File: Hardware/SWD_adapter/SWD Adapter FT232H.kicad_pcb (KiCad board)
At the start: 2 copper layers, 25 parts, among them P2 JUMPER, P3 CONN_JTAGSWD

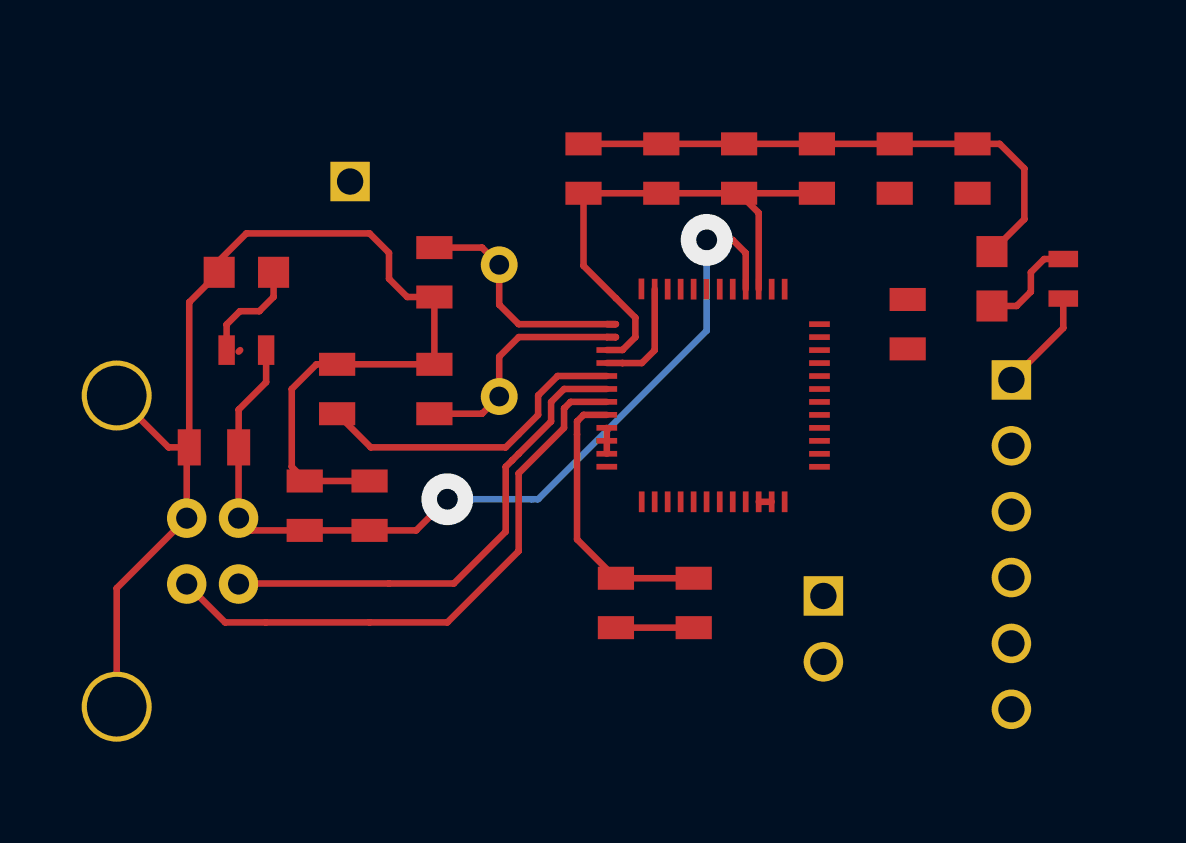
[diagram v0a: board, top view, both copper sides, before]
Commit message: [HARDWARE][SWD_adapter]schema+routage
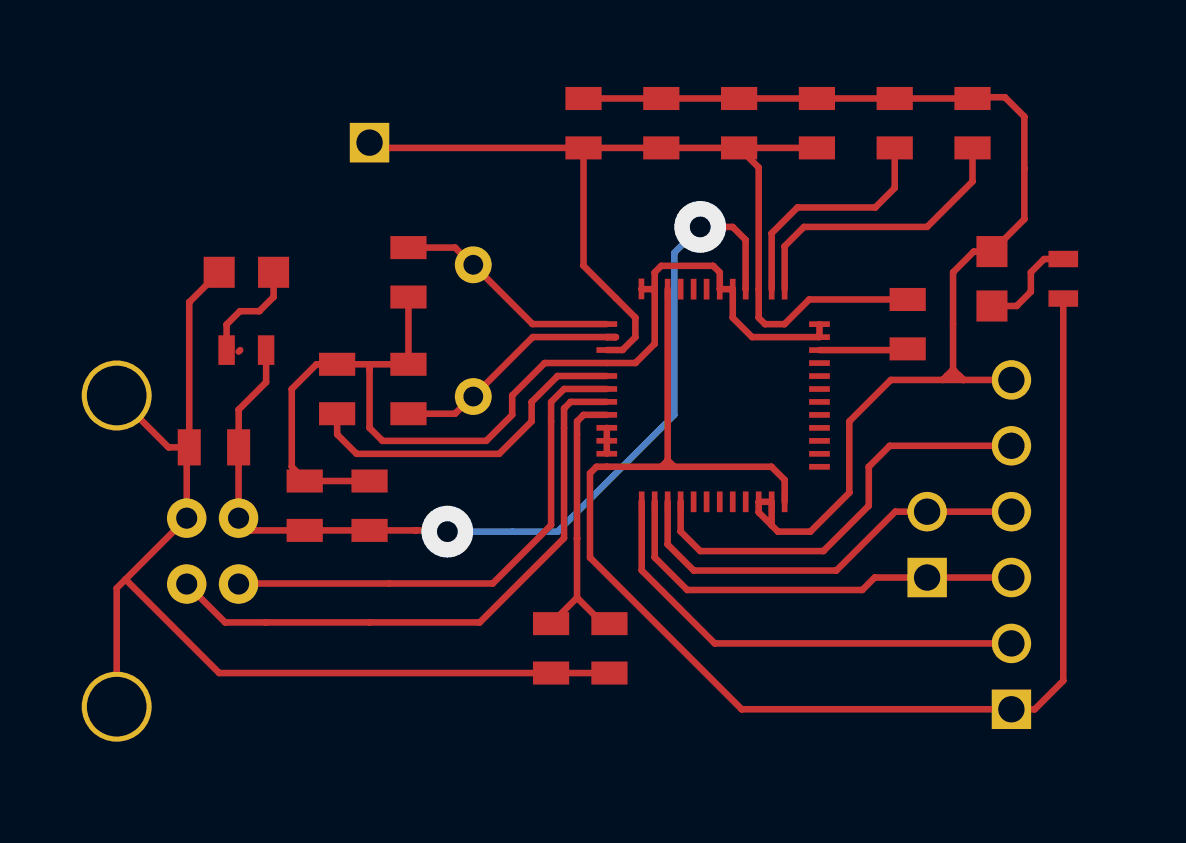
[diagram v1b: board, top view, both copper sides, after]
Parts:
- moved P2 5.15 mm to (77.8, 67.8), turned to 90 degrees
- moved C1 3.69 mm to (65.5, 71.8)
- moved CP1 3.05 mm to (63.2, 71.8)
- moved C2 1.75 mm to (67.5, 51.5)
- moved C4 1.75 mm to (73.5, 51.5)
- moved CP2 1.75 mm to (64.5, 51.5)
- moved CP4 1.75 mm to (70.5, 51.5)
- moved C_VCCA1 1.75 mm to (79.5, 51.5)
- moved C_VCORE1 1.75 mm to (76.5, 51.5)
- moved Pinout_3V3 1.68 mm to (56.2, 52.2)
- moved C_Crystal1 1.00 mm to (57.8, 57.2)
- moved C_Crystal2 1.00 mm to (57.8, 61.8)
- moved Xtal1 1.00 mm to (60.2, 59.5)
- turned P3 to 90 degrees
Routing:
- net GND: track 77.6 -> 131.3 mm
- net /BOARD_3V3: track 3.97 -> 55.3 mm
- net /VCCD_3V3: track 31.6 -> 51.1 mm
- net /TCK: track 0.00 -> 18.1 mm
- net /TMS: track 0.00 -> 16.8 mm
- net /TDI: track 0.00 -> 16.6 mm
- net /TDO: track 0.00 -> 16.3 mm
- net N-000003: track 0.00 -> 11.2 mm
- net N-000002: track 0.00 -> 9.17 mm
- net N-000001: track 0.00 -> 3.42 mm
- net /VBUS_5V: track 35.0 -> 37.4 mm
- net N-000006: track 19.2 -> 20.1 mm
- net N-000009: track 22.5 -> 23.3 mm
- net N-000004: track 12.5 -> 13.2 mm
- net N-0000030: track 9.48 -> 8.87 mm

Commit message: [HARDWARE][SWD_Adapter]routage a verifier
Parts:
- added D1: ESDSUPPRESSOR, LED-0603, F.Cu at (52.5, 72.0)
- added D2: ESDSUPPRESSOR, LED-0603, F.Cu at (54.5, 69.5)
- C1, C2, C3, C4, C_Crystal1, C_Crystal2, C_VBUS1, C_VCCA1, C_VCORE1, R_REF1, R_Reset1: footprint SM0805 -> SM0603
- moved R_Reset1 1.25 mm to (76.2, 58.2)
- moved Pinout_3V3 0.79 mm to (56.0, 53.0)
- moved LED2 0.50 mm to (51.5, 57.8)
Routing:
- net GND: track 131.3 -> 292.3 mm, vias 0 -> 4
- net /VBUS_5V: track 37.4 -> 45.6 mm
- net /VCCD_3V3: track 51.1 -> 55.1 mm
- net N-000008: track 20.1 -> 20.9 mm
- net N-000009: track 23.3 -> 23.8 mm
- net N-0000011: track 4.19 -> 3.69 mm
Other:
- net class BOARD_3V3 added: clearance 0.2, trace_width 0.5, via_dia 2, via_drill 0.8
- net class GND added: clearance 0.2, trace_width 0.5, via_dia 2, via_drill 0.8
- net class VCC_3V3 added: clearance 0.2, trace_width 0.5, via_dia 2, via_drill 0.8
- net class VUSB-5V added: clearance 0.2, trace_width 0.5, via_dia 2, via_drill 0.8

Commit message: [HARDWARE][SWD_Adapter]Ajout des plans de masse
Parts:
- Pinout_3V3: moved to B.Cu
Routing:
- added copper zone on B.Cu, net GND
- added copper zone on F.Cu, net GND
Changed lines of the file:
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@@
     (links 72)
     (no_connects 0)
-    (area 35.949499 49.021479 85.069266 75.9724)
+    (area 35.949499 48.75 85.250001 77.250001)
     (thickness 1.6)
     (drawings 0)
-    (tracks 319)
+    (tracks 318)
     (zones 0)
     (modules 27)
@@
     )
   )
-  (module PIN_ARRAY_1 (layer Dessus.Cu)
+  (module PIN_ARRAY_1 (layer Dessous.Cu)
     (at 56 53)
     (descr "1 pin")
     (tags "CONN DEV")
-    (fp_text reference Pinout_3V3 (at 0 -1.905) (layer Dessus.SilkS)
-      (effects (font (size 0.762 0.762) (thickness 0.1524)))
-    )
-    (fp_text value CONN_1 (at 0 -1.905) (layer Dessus.SilkS) hide
-      (effects (font (size 0.762 0.762) (thickness 0.1524)))
-    )
-    (fp_line (start 1.27 1.27) (end -1.27 1.27) (layer Dessus.SilkS) (width 0.1524))
-    (fp_line (start -1.27 -1.27) (end 1.27 -1.27) (layer Dessus.SilkS) (width 0.1524))
-    (fp_line (start -1.27 1.27) (end -1.27 -1.27) (layer Dessus.SilkS) (width 0.1524))
-    (fp_line (start 1.27 -1.27) (end 1.27 1.27) (layer Dessus.SilkS) (width 0.1524))
+    (fp_text reference Pinout_3V3 (at 0 1.905) (layer Dessous.SilkS)
+      (effects (font (size 0.762 0.762) (thickness 0.1524)) (justify mirror))
+    )
+    (fp_text value CONN_1 (at 0 1.905) (layer Dessous.SilkS) hide
+      (effects (font (size 0.762 0.762) (thickness 0.1524)) (justify mirror))
+    )
+    (fp_line (start 1.27 -1.27) (end -1.27 -1.27) (layer Dessous.SilkS) (width 0.1524))
+    (fp_line (start -1.27 1.27) (end 1.27 1.27) (layer Dessous.SilkS) (width 0.1524))
+    (fp_line (start -1.27 -1.27) (end -1.27 1.27) (layer Dessous.SilkS) (width 0.1524))
+    (fp_line (start 1.27 1.27) (end 1.27 -1.27) (layer Dessous.SilkS) (width 0.1524))
     (pad 1 thru_hole rect (at 0 0) (size 1.524 1.524) (drill 1.016)
-      (layers *.Cu *.Mask Dessus.SilkS)
+      (layers *.Cu *.Mask Dessous.SilkS)
       (net 7 /VCCD_3V3)
     )
@@
     )
   )
-  (segment (start 51.2025 60.3095) (end 51.262 60.25) (width 0.254) (layer Dessus.Cu) (net 0))
   (segment (start 81 74.1) (end 81.9 74.1) (width 0.254) (layer Dessus.Cu) (net 1))
   (segment (start 83 73) (end 83 58.262) (width 0.254) (layer Dessus.Cu) (net 1))
@@
   (segment (start 63.5 67.25) (end 68 62.75) (width 0.5) (layer Dessous.Cu) (net 6))
   (segment (start 59.25 67.25) (end 63.5 67.25) (width 0.5) (layer Dessous.Cu) (net 6))
-  (segment (start 51.199 66.73) (end 51.23 66.73) (width 0.5) (layer Dessus.Cu) (net 6) (status C00000))
-  (segment (start 51.23 66.73) (end 51.75 67.25) (width 0.5) (layer Dessus.Cu) (net 6) (status C00000))
-  (segment (start 51.75 67.25) (end 59.25 67.25) (width 0.5) (layer Dessus.Cu) (net 6) (status 400000))
+  (segment (start 51.199 66.73) (end 51.23 66.73) (width 0.5) (layer Dessus.Cu) (net 6))
+  (segment (start 51.23 66.73) (end 51.75 67.25) (width 0.5) (layer Dessus.Cu) (net 6))
+  (segment (start 51.75 67.25) (end 59.25 67.25) (width 0.5) (layer Dessus.Cu) (net 6))
   (segment (start 59.2025 67.2025) (end 59.25 67.25) (width 0.254) (layer Dessus.Cu) (net 6))
   (via (at 59.25 67.25) (size 2) (layers Dessus.Cu Dessous.Cu) (net 6))
@@
   (segment (start 68.5 72.75) (end 76.75 64.5) (width 0.5) (layer Dessous.Cu) (net 8))
   (segment (start 58 72.75) (end 68.5 72.75) (width 0.5) (layer Dessous.Cu) (net 8))
-  (segment (start 81 61.4) (end 76.85 61.4) (width 0.5) (layer Dessus.Cu) (net 8) (status 400000))
+  (segment (start 81 61.4) (end 76.85 61.4) (width 0.5) (layer Dessus.Cu) (net 8))
   (segment (start 76.85 61.4) (end 76.75 61.5) (width 0.5) (layer Dessus.Cu) (net 8))
   (segment (start 78.75 57.25) (end 78.75 61) (width 0.5) (layer Dessus.Cu) (net 8))
@@
   (segment (start 51.0007 71.2507) (end 52.5 71.2507) (width 0.254) (layer Dessus.Cu) (net 18))
   (segment (start 49.20002 69.45002) (end 51.0007 71.2507) (width 0.254) (layer Dessus.Cu) (net 18))
+  (zone (net 8) (net_name GND) (layer Dessus.Cu) (hatch edge 0.508)
+    (connect_pads (clearance 0.508))
+    (min_thickness 0.254)
+    (fill (arc_segments 16) (thermal_gap 0.508) (thermal_bridge_width 0.508))
+    (polygon
+      (pts
+        (xy 85.25 77.25) (xy 44.5 77.25) (xy 44.5 48.75) (xy 85.25 48.75)
+      )
+    )
+  )
+  (zone (net 8) (net_name GND) (layer Dessous.Cu) (hatch edge 0.508)
+    (connect_pads (clearance 0.508))
+    (min_thickness 0.254)
+    (fill (arc_segments 16) (thermal_gap 0.508) (thermal_bridge_width 0.508))
+    (polygon
+      (pts
+        (xy 85.25 77.25) (xy 44.5 77.25) (xy 44.5 48.75) (xy 85.25 48.75)
+      )
+    )
+  )
 )

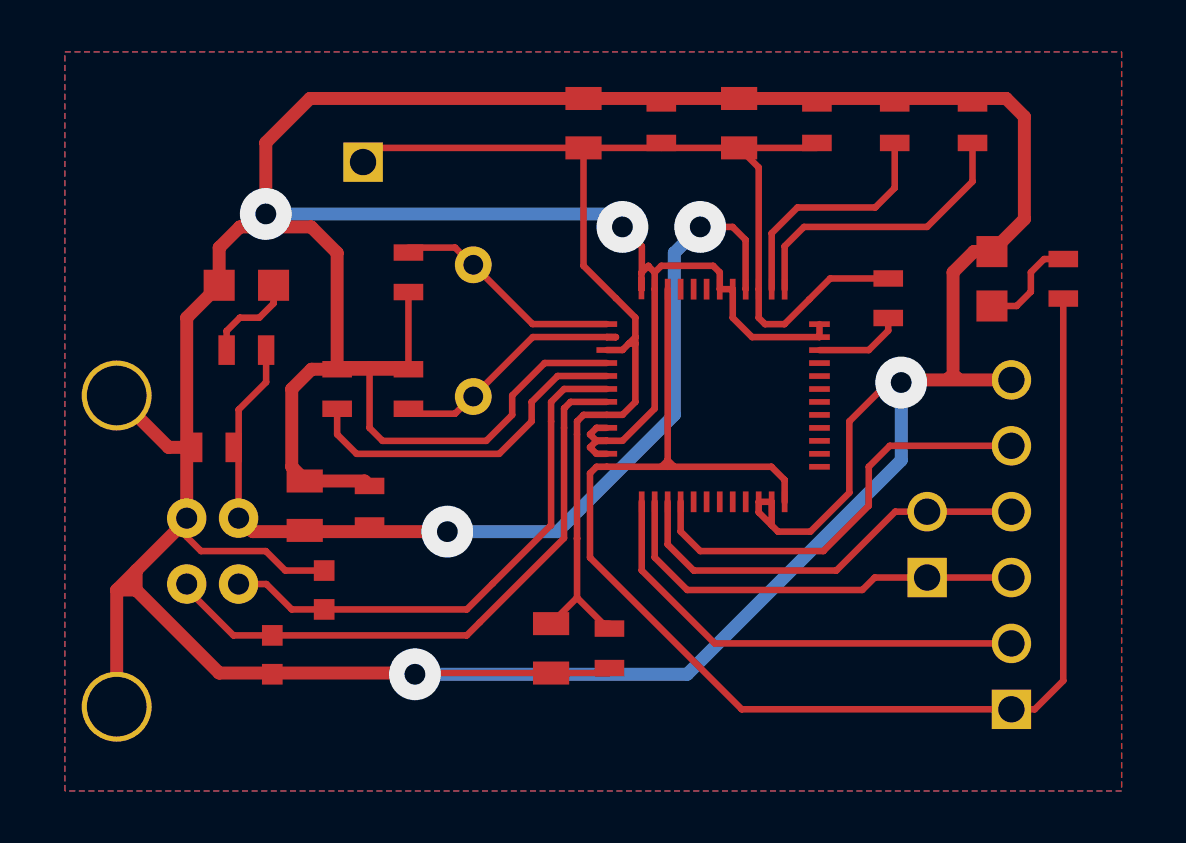
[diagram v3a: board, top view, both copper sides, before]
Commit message: [HARDWARE][SWD_Adapter]Routage: capa de decouplage plus proches des pins
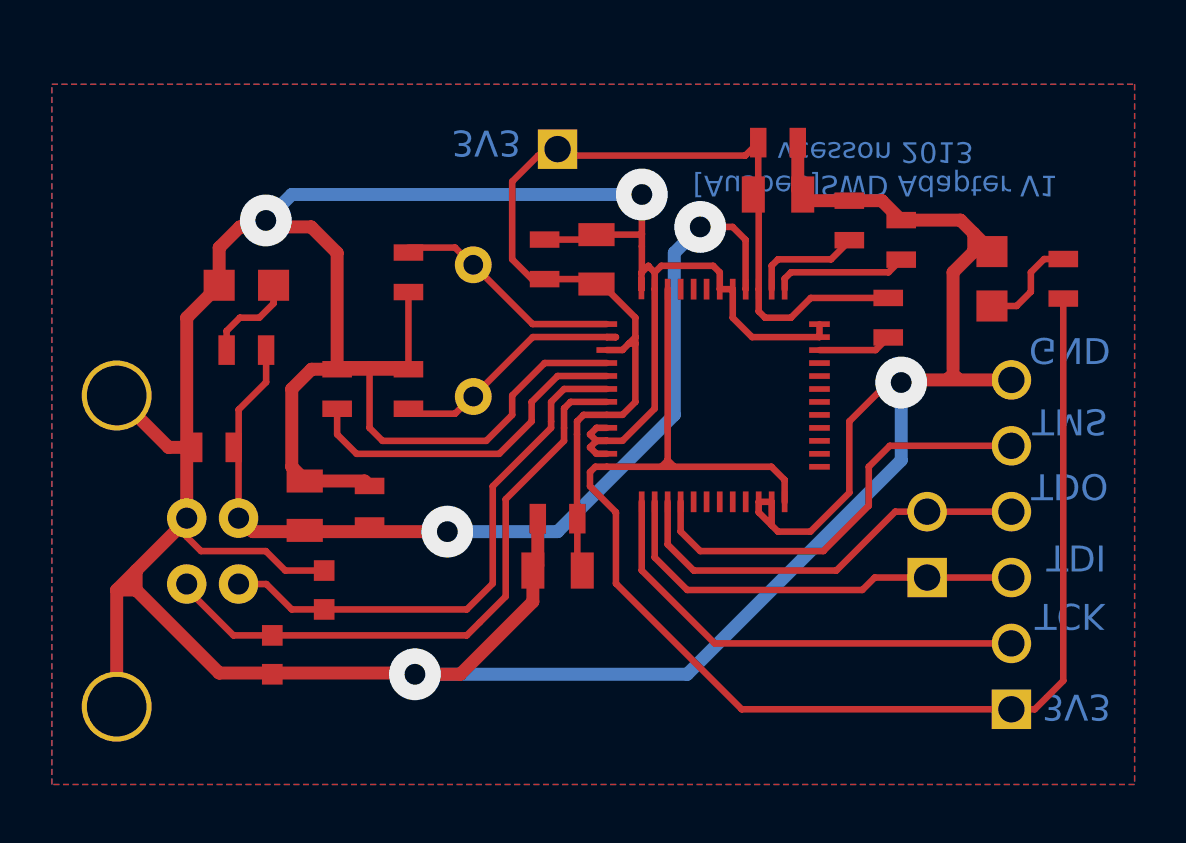
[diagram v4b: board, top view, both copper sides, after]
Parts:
- moved Pinout_3V3 7.52 mm to (63.5, 52.5)
- moved C2 6.91 mm to (63.0, 56.8)
- moved C1 5.39 mm to (63.5, 66.8), turned to 180 degrees
- moved C_VCCA1 5.27 mm to (76.8, 56.0)
- moved CP2 5.27 mm to (65.0, 56.8)
- moved C_VCORE1 4.14 mm to (74.8, 55.2)
- moved CP4 3.13 mm to (72.0, 54.2), turned to 0 degrees
- moved CP1 3.01 mm to (63.5, 68.8), turned to 180 degrees
- moved C4 1.68 mm to (72.0, 52.2), turned to 0 degrees
- moved R_Reset1 0.75 mm to (76.2, 59.0)
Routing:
- net GND: track 292.3 -> 253.5 mm
- net /VCCD_3V3: track 55.1 -> 44.1 mm
- net N-000004: track 11.2 -> 5.20 mm
- net N-000001: track 9.17 -> 4.33 mm
- net N-000002: track 3.45 -> 2.85 mm
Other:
- board text added: "3V3"
- board text added: "GND"
- board text added: "TCK"
- board text added: "TDI"
- board text added: "TDO"
- board text added: "TMS"
- board text added: "[Ausbee]SWD Adapter V1 vcesson 2013"

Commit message: [HARDWARE][SWD_Adapter]correction de routage
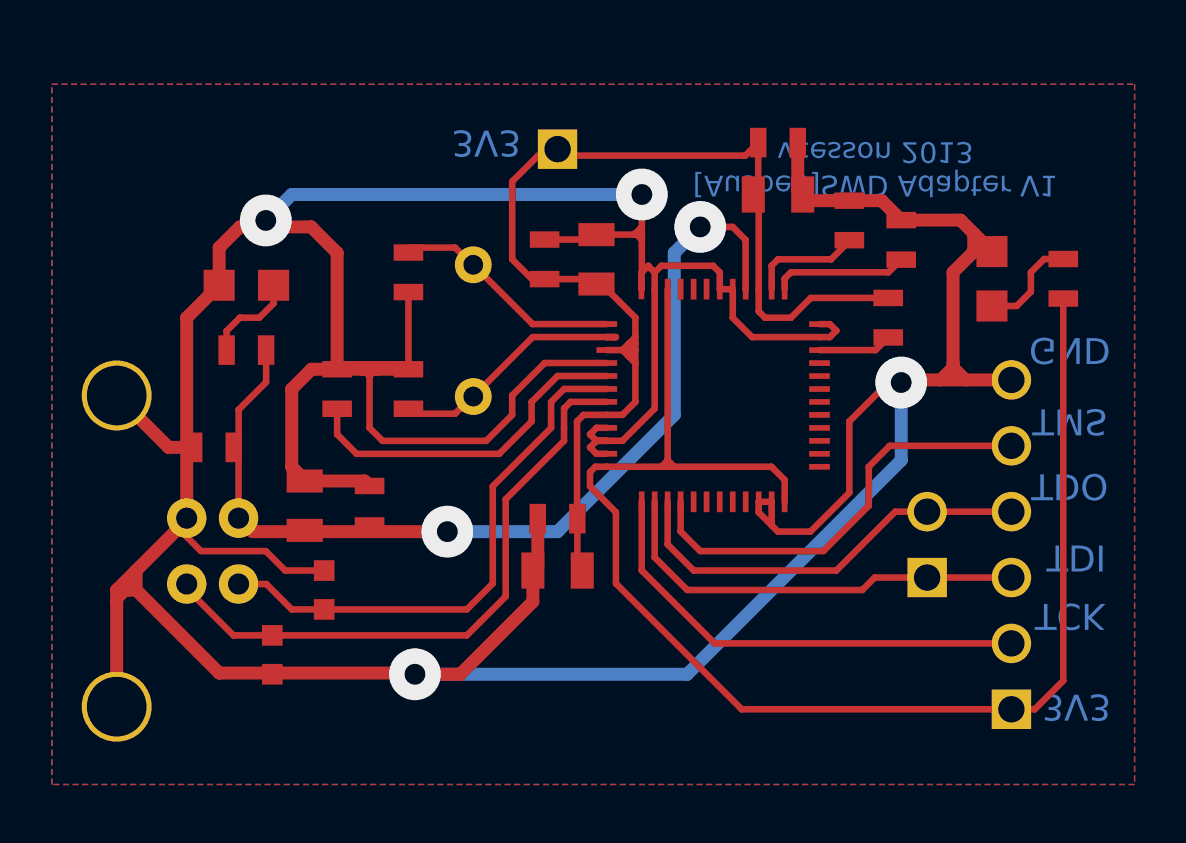
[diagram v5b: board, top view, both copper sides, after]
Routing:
- net GND: track 253.5 -> 258.4 mm
- net /VCCD_3V3: track 44.1 -> 45.8 mm
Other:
- net class BOARD_3V3: trace_width 0.5 -> 0.254
- net class GND: trace_width 0.5 -> 0.254
- net class VCC_3V3: trace_width 0.5 -> 0.254
- net class VUSB-5V: trace_width 0.5 -> 0.254
